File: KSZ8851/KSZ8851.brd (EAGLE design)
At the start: 50 x 30 mm, 53 parts, among them IC1 AT93C46A-10SQ-2.7, P1 RB1-125BAG1A

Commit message: Fix angle wire angle and add power LED
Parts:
- C5, C6: value 0.1uF -> 18pF
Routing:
- net GND: track 45.0 -> 42.5 mm
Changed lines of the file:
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@@
 <grid distance="0.1" unitdist="mm" unit="mm" style="lines" multiple="1" display="no" altdistance="0.01" altunitdist="mm" altunit="mm"/>
 <layers>
-<layer number="1" name="Top" color="4" fill="1" visible="no" active="yes"/>
+<layer number="1" name="Top" color="4" fill="1" visible="yes" active="yes"/>
 <layer number="2" name="Route2" color="1" fill="3" visible="no" active="no"/>
 <layer number="3" name="Route3" color="4" fill="3" visible="no" active="no"/>
@@
 <layer number="19" name="Unrouted" color="14" fill="1" visible="yes" active="yes"/>
 <layer number="20" name="Dimension" color="15" fill="1" visible="yes" active="yes"/>
-<layer number="21" name="tPlace" color="7" fill="1" visible="no" active="yes"/>
+<layer number="21" name="tPlace" color="7" fill="1" visible="yes" active="yes"/>
 <layer number="22" name="bPlace" color="7" fill="1" visible="yes" active="yes"/>
-<layer number="23" name="tOrigins" color="15" fill="1" visible="no" active="yes"/>
+<layer number="23" name="tOrigins" color="15" fill="1" visible="yes" active="yes"/>
 <layer number="24" name="bOrigins" color="15" fill="1" visible="yes" active="yes"/>
-<layer number="25" name="tNames" color="7" fill="1" visible="no" active="yes"/>
+<layer number="25" name="tNames" color="7" fill="1" visible="yes" active="yes"/>
 <layer number="26" name="bNames" color="7" fill="1" visible="yes" active="yes"/>
 <layer number="27" name="tValues" color="7" fill="1" visible="no" active="yes"/>
@@
 <layer number="49" name="Reference" color="7" fill="1" visible="no" active="yes"/>
 <layer number="50" name="dxf" color="7" fill="1" visible="no" active="yes"/>
-<layer number="51" name="tDocu" color="7" fill="1" visible="no" active="yes"/>
+<layer number="51" name="tDocu" color="7" fill="1" visible="yes" active="yes"/>
 <layer number="52" name="bDocu" color="7" fill="1" visible="yes" active="yes"/>
 <layer number="53" name="tGND_GNDA" color="7" fill="1" visible="no" active="yes"/>
@@
 <element name="R9" library="rcl" package="R0603" value="4.7K" x="32.089" y="27.617" rot="R270"/>
 <element name="-25.000MHZMAAJ-T1" library="crystal" package="SMD2.5X2" value="8Z-25.000MHZMAAJ-T" x="29.207" y="7.794" rot="R180"/>
-<element name="C5" library="rcl" package="C0603" value="0.1uF" x="26.5" y="7.7" rot="R270"/>
-<element name="C6" library="rcl" package="C0603" value="0.1uF" x="31.96" y="7.46" rot="R270"/>
+<element name="C5" library="rcl" package="C0603" value="18pF" x="26.5" y="7.7" rot="R270"/>
+<element name="C6" library="rcl" package="C0603" value="18pF" x="31.96" y="7.46" rot="R270"/>
 <element name="JP1" library="pinhead" package="2X05" value="" x="47.384" y="15.1" rot="R90"/>
 <element name="R10" library="rcl" package="R0603" value="4.7K" x="35.649" y="20.56" rot="R270"/>
@@
 <wire x1="43.138" y1="9.535" x2="45.629" y2="9.535" width="0.4064" layer="1"/>
 <wire x1="45.629" y1="9.535" x2="46.114" y2="10.02" width="0.4064" layer="1"/>
-<wire x1="37.637" y1="6.965" x2="35.125" y2="6.965" width="0.4064" layer="1"/>
 <wire x1="35.125" y1="6.965" x2="35.11" y2="6.98" width="0.4064" layer="1"/>
 <via x="35.11" y="6.98" extent="1-16" drill="0.5"/>
@@
 <contactref element="SJ3" pad="2"/>
 <contactref element="SJ4" pad="2"/>
+<wire x1="35.125" y1="6.965" x2="37.637" y2="6.965" width="0" layer="19" extent="1-1"/>
 </signal>
 <signal name="N$1">

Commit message: Generate gerber file
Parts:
- added LED1: Green, led:SML0603
- added R13: 1.5k, rcl:R0603
- moved C8 0.07 mm to (37.7, 8.44), turned to 90 degrees
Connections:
- new net N$4: LED1.A, R13.2
- net +3V3: now also R13.1
- net GND: now also LED1.C
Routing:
- net GND: track 42.5 -> 46.7 mm, vias 13 -> 14
- net N$4: track 0.00 -> 1.40 mm

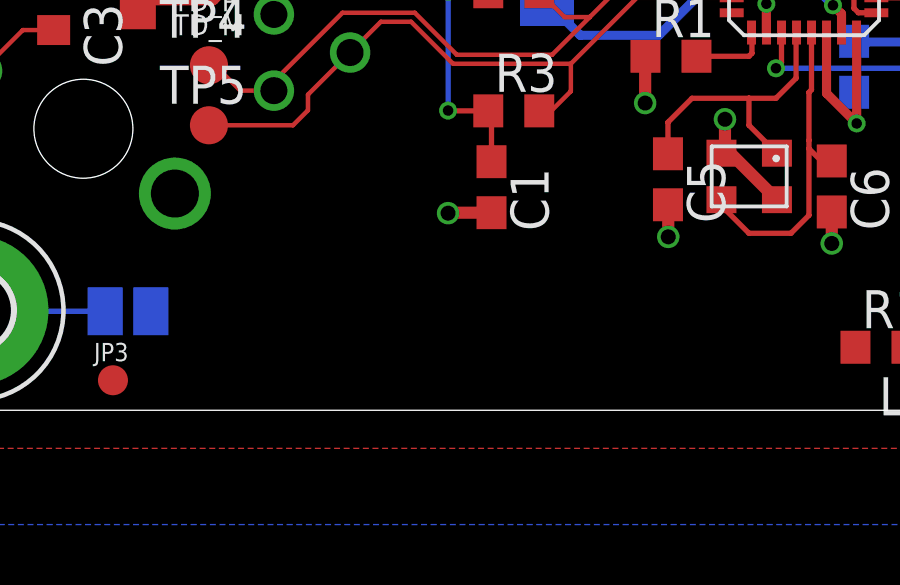
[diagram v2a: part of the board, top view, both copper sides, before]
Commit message: Add Exmachina logo and CC
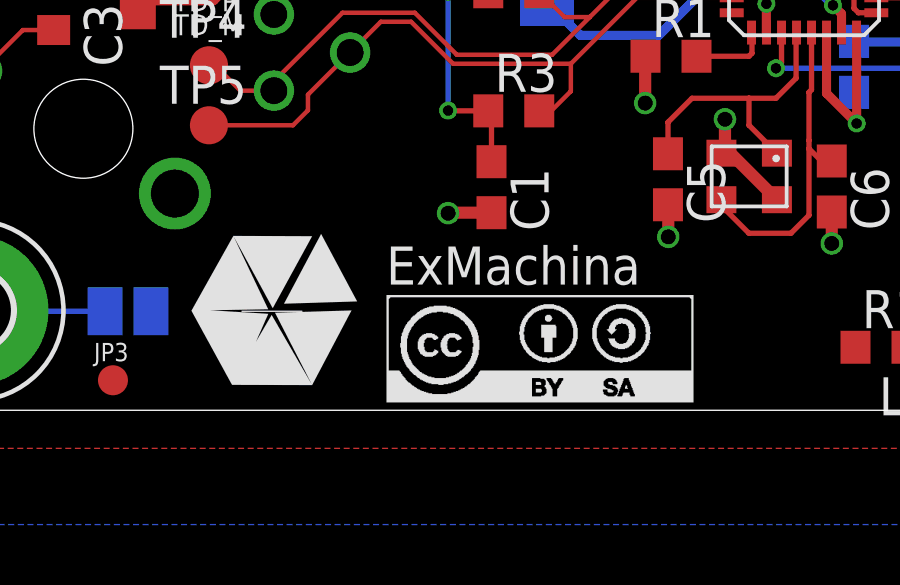
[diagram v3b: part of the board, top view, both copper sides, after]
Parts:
- added U$2: EXMACHINA-LOGO-NAME, exmachina:EXM-LOGO-BASELINE
- added U$3: CC-BY-SA, cc-by-sa:CC-BY-SA
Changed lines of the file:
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@@
 <layer number="23" name="tOrigins" color="15" fill="1" visible="yes" active="yes"/>
 <layer number="24" name="bOrigins" color="15" fill="1" visible="yes" active="yes"/>
-<layer number="25" name="tNames" color="7" fill="1" visible="yes" active="yes"/>
-<layer number="26" name="bNames" color="7" fill="1" visible="yes" active="yes"/>
+<layer number="25" name="tNames" color="7" fill="1" visible="no" active="yes"/>
+<layer number="26" name="bNames" color="7" fill="1" visible="no" active="yes"/>
 <layer number="27" name="tValues" color="7" fill="1" visible="no" active="yes"/>
 <layer number="28" name="bValues" color="7" fill="1" visible="no" active="yes"/>
@@
 <layer number="37" name="tTest" color="7" fill="1" visible="no" active="yes"/>
 <layer number="38" name="bTest" color="7" fill="1" visible="no" active="yes"/>
-<layer number="39" name="tKeepout" color="4" fill="11" visible="yes" active="yes"/>
-<layer number="40" name="bKeepout" color="1" fill="11" visible="yes" active="yes"/>
-<layer number="41" name="tRestrict" color="4" fill="10" visible="yes" active="yes"/>
-<layer number="42" name="bRestrict" color="1" fill="10" visible="yes" active="yes"/>
-<layer number="43" name="vRestrict" color="2" fill="10" visible="yes" active="yes"/>
+<layer number="39" name="tKeepout" color="4" fill="11" visible="no" active="yes"/>
+<layer number="40" name="bKeepout" color="1" fill="11" visible="no" active="yes"/>
+<layer number="41" name="tRestrict" color="4" fill="10" visible="no" active="yes"/>
+<layer number="42" name="bRestrict" color="1" fill="10" visible="no" active="yes"/>
+<layer number="43" name="vRestrict" color="2" fill="10" visible="no" active="yes"/>
 <layer number="44" name="Drills" color="7" fill="1" visible="no" active="yes"/>
 <layer number="45" name="Holes" color="7" fill="1" visible="no" active="yes"/>
@@
 <layer number="49" name="Reference" color="7" fill="1" visible="no" active="yes"/>
 <layer number="50" name="dxf" color="7" fill="1" visible="no" active="yes"/>
-<layer number="51" name="tDocu" color="7" fill="1" visible="yes" active="yes"/>
-<layer number="52" name="bDocu" color="7" fill="1" visible="yes" active="yes"/>
+<layer number="51" name="tDocu" color="7" fill="1" visible="no" active="yes"/>
+<layer number="52" name="bDocu" color="7" fill="1" visible="no" active="yes"/>
 <layer number="53" name="tGND_GNDA" color="7" fill="1" visible="no" active="yes"/>
 <layer number="54" name="bGND_GNDA" color="7" fill="1" visible="no" active="yes"/>
@@
 <element name="LED1" library="led" package="SML0603" value="Green" x="36.6" y="2.1" rot="R180"/>
 <element name="R13" library="rcl" package="R0603" value="1.5k" x="33.6" y="2.1"/>
+<element name="U$2" library="exmachina" package="EXM-LOGO-BASELINE" value="EXMACHINA-LOGO-NAME" x="13.3" y="3.3"/>
+<element name="U$3" library="cc-by-sa" package="CC-BY-SA" value="CC-BY-SA" x="22.4" y="2.5"/>
 </elements>
 <signals>

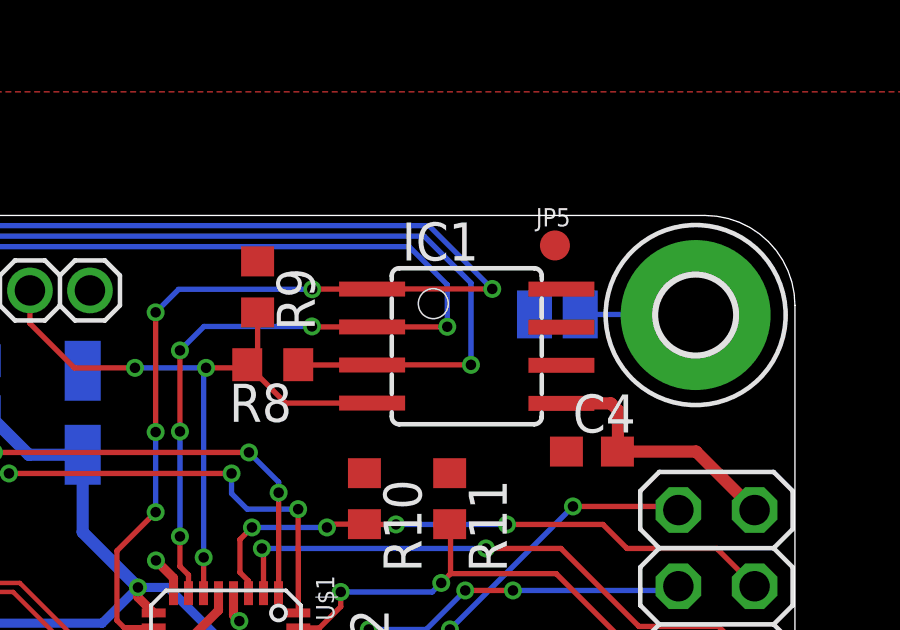
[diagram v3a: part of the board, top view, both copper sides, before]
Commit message: Add BOM to KSZ8851 board and place component name on the board
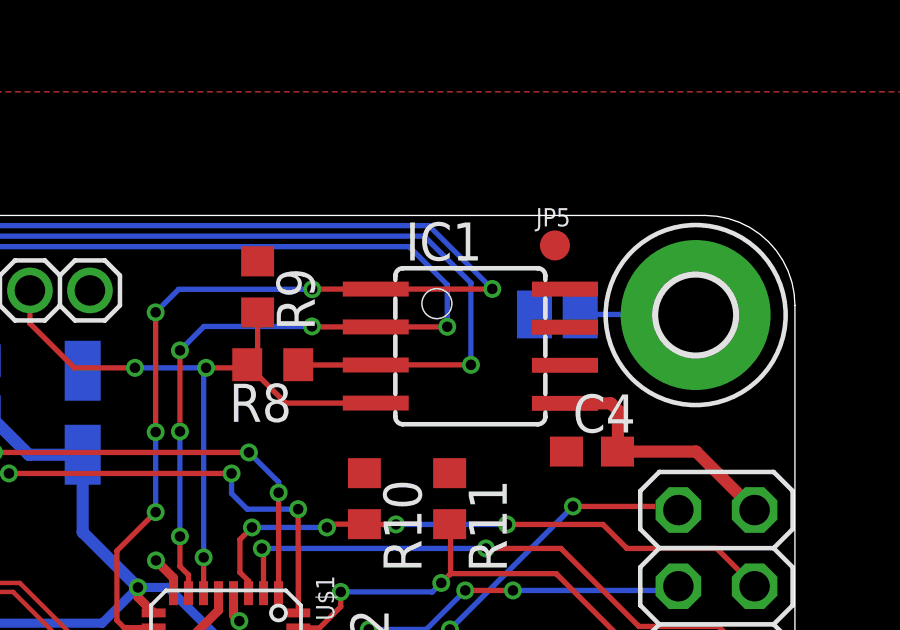
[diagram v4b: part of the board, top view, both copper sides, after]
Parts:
- IC1: value AT93C46A-10SQ-2.7 -> AT93C46EN-SH-BSOIC8
- moved IC1 0.12 mm to (39.2, 25.6)
